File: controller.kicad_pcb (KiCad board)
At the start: 2 copper layers, 156.8 x 70.7 mm, 46 parts, among them J1 Conn_ST_STDC14, J2 USB_C_Receptacle_USB2.0_14P, SW1 SW_Push, SW10 SW_Push, SW11 SW_Push, SW2 SW_Push, SW3 SW_Push, SW4 SW_Push, SW5 SW_Push, SW6 SW_Push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

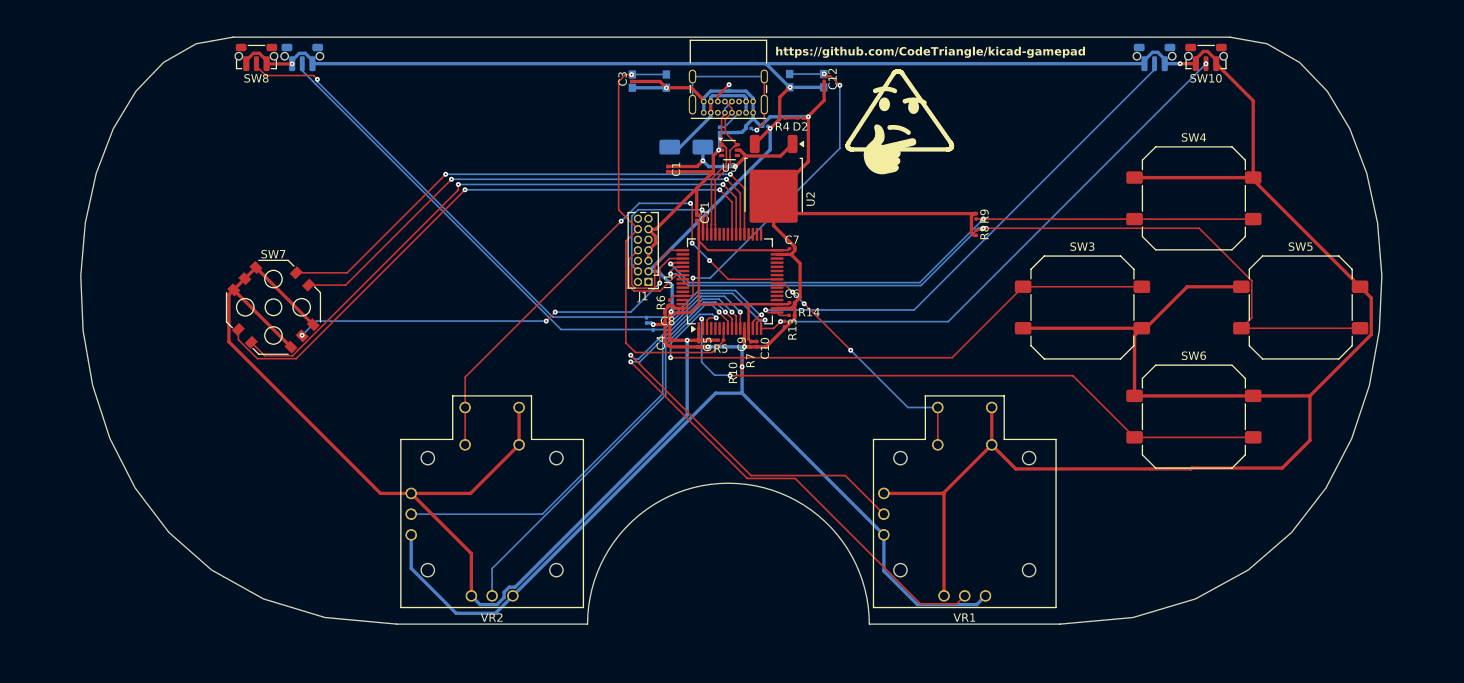
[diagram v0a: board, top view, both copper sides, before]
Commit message: add start and select + resistors to all other buttons
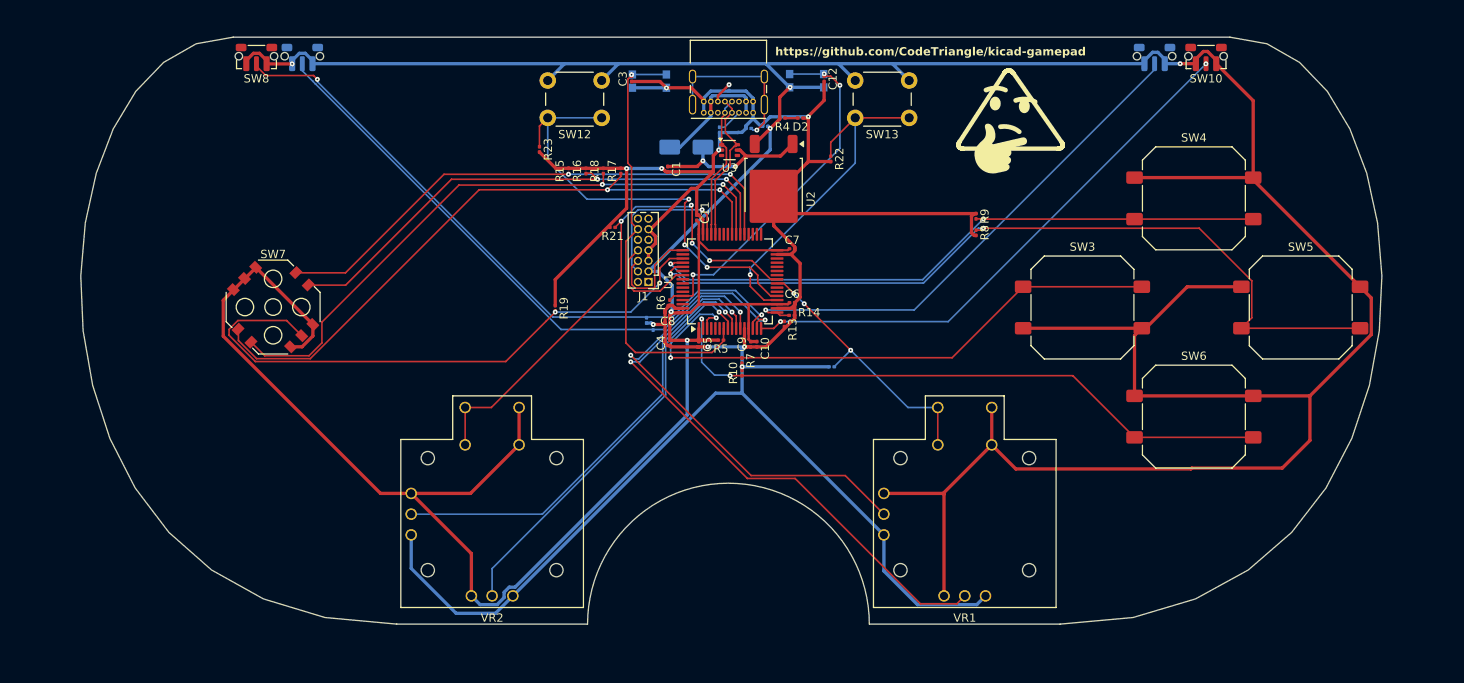
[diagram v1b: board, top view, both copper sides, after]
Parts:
- added R15: 10k, Resistor_SMD:R_0201_0603Metric, F.Cu at (118.0, 78.3)
- added R16: 10k, Resistor_SMD:R_0201_0603Metric, F.Cu at (120.1, 78.3)
- added R17: 10k, Resistor_SMD:R_0201_0603Metric, F.Cu at (124.3, 78.3)
- added R18: 10k, Resistor_SMD:R_0201_0603Metric, F.Cu at (122.2, 78.3)
- added R19: 10k, Resistor_SMD:R_0201_0603Metric, F.Cu at (116.4, 94.8)
- added R20: 10k, Resistor_SMD:R_0201_0603Metric, B.Cu at (149.7, 101.9)
- added R21: 10k, Resistor_SMD:R_0201_0603Metric, F.Cu at (123.3, 85.1)
- added R22: 10k, Resistor_SMD:R_0201_0603Metric, F.Cu at (149.6, 76.8)
- added R23: 10k, Resistor_SMD:R_0201_0603Metric, F.Cu at (114.5, 75.7)
- added SW12: SW_Push, Button_Switch_THT:SW_PUSH_6mm, F.Cu at (122.0, 71.9)
- added SW13: SW_Push, Button_Switch_THT:SW_PUSH_6mm, F.Cu at (159.0, 71.9)
- moved SW7 0.05 mm to (82.4, 94.7)
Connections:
- R7 pad 1: ButtonLeft -> GND
- R7 pad 2: GND -> ButtonLeft
- U1 pad 20: SelectINS -> ButtonStart
- U1 pad 21: SPI1_SCK -> ButtonSelect
- U1 pad 22: SPI1_MISO -> unconnected-(U1-PA6-Pad22)
- U1 pad 23: SPI1_MOSI -> unconnected-(U1-PA7-Pad23)
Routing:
- net ButtonSelect: track 0.00 -> 54.4 mm, vias 0 -> 3
- net GND: track 270.2 -> 320.1 mm, vias 7 -> 9
- net ButtonStart: track 0.00 -> 41.8 mm, vias 0 -> 1
- net DPadCenter: track 50.7 -> 72.8 mm, vias 4 -> 2
- net +3.3V: track 566.1 -> 573.0 mm
- net RightClick: track 30.1 -> 32.8 mm
- net DPadLeft: track 74.6 -> 77.2 mm
- net LeftClick: track 60.9 -> 63.5 mm
- net DPadDown: track 73.2 -> 75.6 mm
- net DPadRight: track 63.0 -> 64.7 mm
- net nRST: track 53.5 -> 52.0 mm

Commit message: fix ERC and add metadata
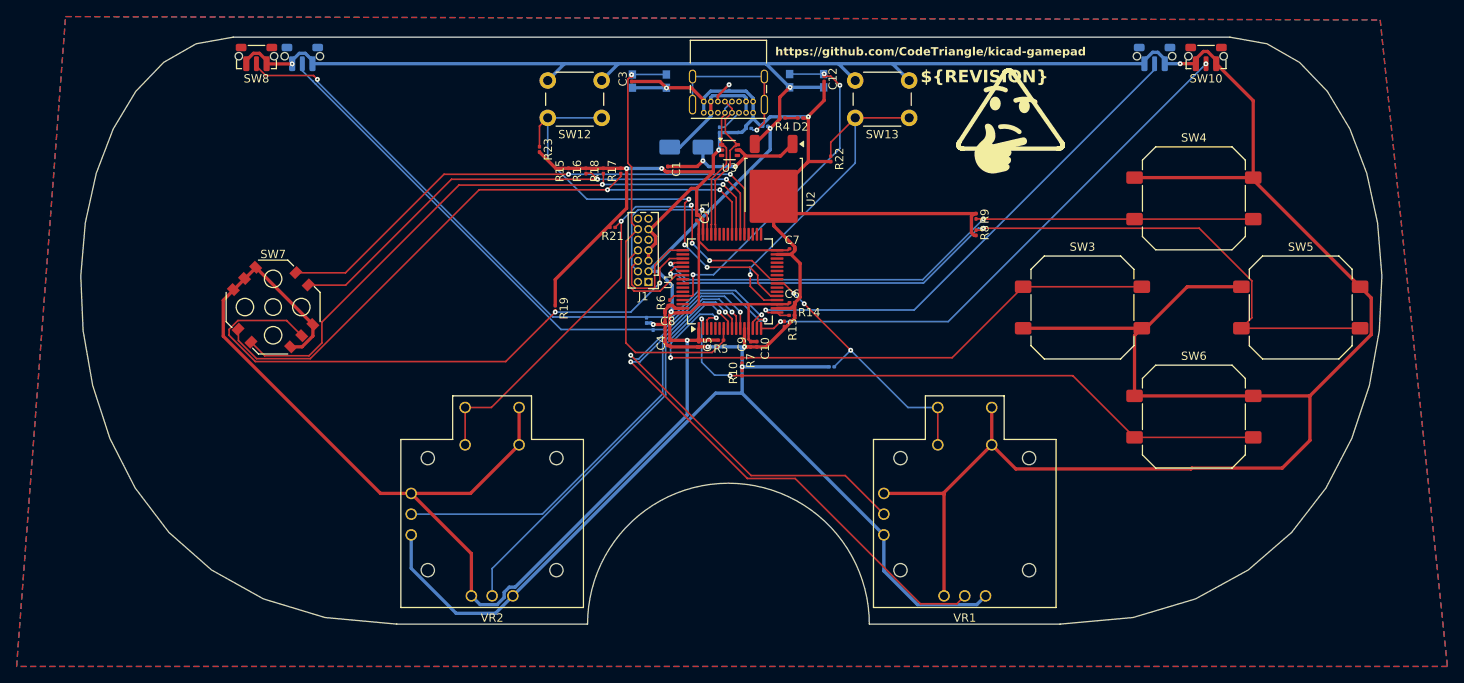
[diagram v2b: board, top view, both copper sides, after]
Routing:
- added copper zone on B.Cu, net GND
- added copper zone on F.Cu, net GND
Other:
- board text added: "${REVISION}"
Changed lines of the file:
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@@
 	)
 	(paper "A4")
+	(title_block
+		(title "${TITLE}")
+		(date "2025-11-02")
+		(rev "${REVISION}")
+		(company "USU")
+		(comment 1 "${AUTHOR}")
+	)
 	(layers
 		(0 "F.Cu" signal)
@@
 		)
 	)
+	(property "AUTHOR" "Richard Snider (CodeTriangle)")
+	(property "REVISION" "R1.0-A")
+	(property "TITLE" "USB Gamepad Controller")
 	(net 0 "")
 	(net 1 "+5V")
@@
 		(layer "Edge.Cuts")
 	)
+	(gr_text "${REVISION}"
+		(at 160.4 67.8 0)
+		(layer "F.SilkS")
+		(effects
+			(font
+				(size 1.5 1.5)
+				(thickness 0.3)
+				(bold yes)
+			)
+			(justify left bottom)
+		)
+	)
 	(gr_text "https://github.com/CodeTriangle/kicad-gamepad"
 		(at 142.9 64.5 0)
@@
 		(net 67)
 	)
+	(zone
+		(net 2)
+		(net_name "GND")
+		(layers "F.Cu" "B.Cu")
+		(hatch edge 0.5)
+		(connect_pads
+			(clearance 0.5)
+		)
+		(min_thickness 0.25)
+		(filled_areas_thickness no)
+		(fill yes
+			(thermal_gap 0.5)
+			(thermal_bridge_width 0.5)
+		)
+		(polygon
+			(pts
+				(xy 57.4 59.7) (xy 215.8 60.1) (xy 223.9 138) (xy 51.5 138)
+			)
+		)
+	)
 	(group ""

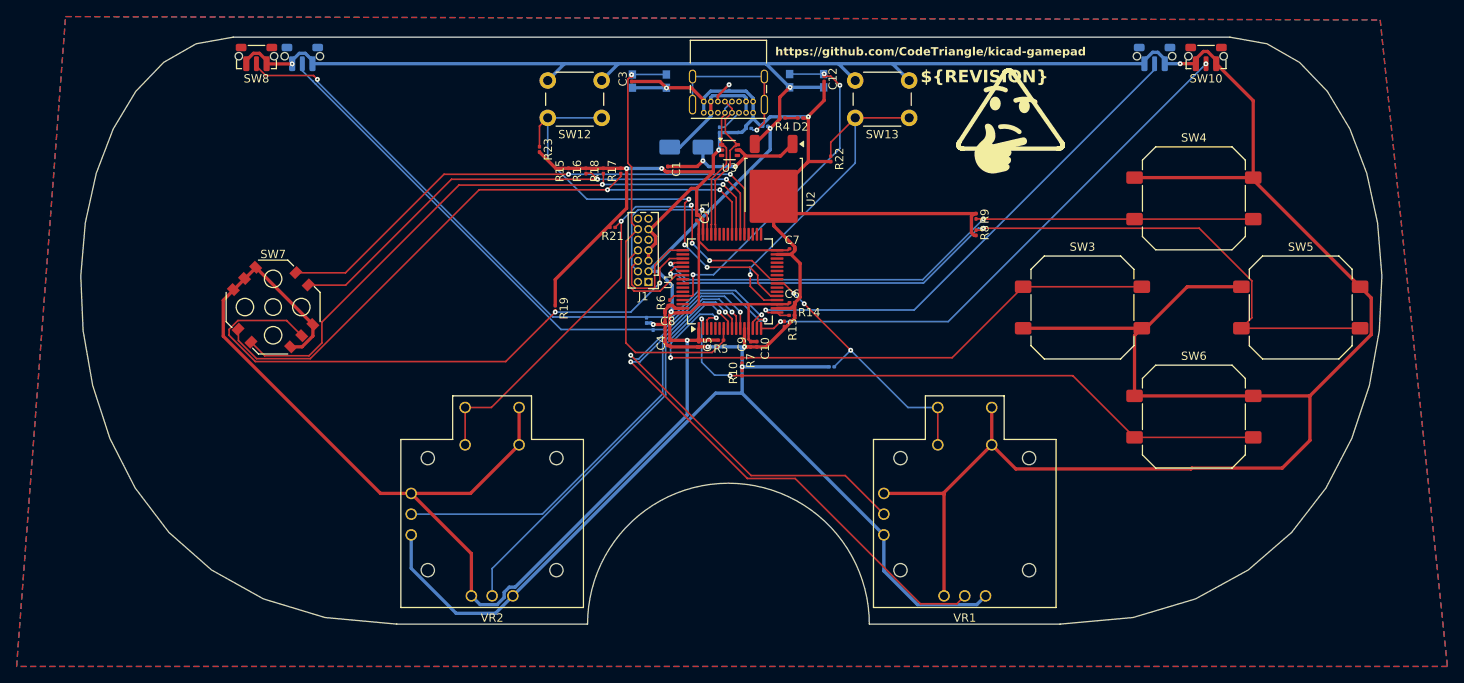
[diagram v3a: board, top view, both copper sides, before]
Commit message: update pcb to reflect new footprints
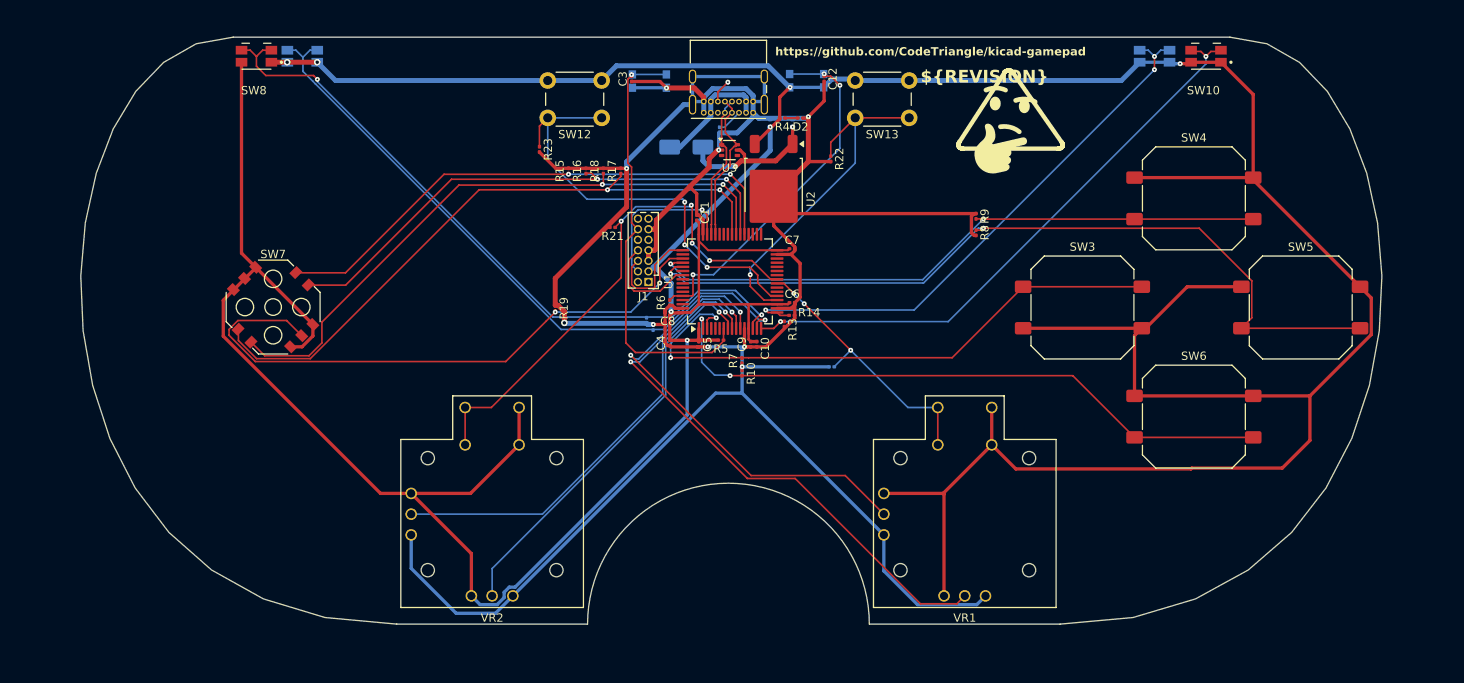
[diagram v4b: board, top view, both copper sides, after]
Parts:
- removed R3: 5.1k, Resistor_SMD:R_0201_0603Metric
- C1: value 10uF -> 10u; footprint Capacitor_SMD:C_0201_0603Metric -> Capacitor_SMD:C_0402_1005Metric; moved to B.Cu
- C12, C3: value 100nF -> 100n
- C2: value 10uF -> 10u; footprint Capacitor_SMD:C_0201_0603Metric -> Capacitor_SMD:C_0402_1005Metric
- SW10, SW11, SW8, SW9: footprint Button_Switch_SMD:SW_Push_1P1T-MP_NO_Horizontal_Alps_SKRTLAE010 -> EVQ-P7A01P:SW_EVQ-P7A01P_Single
- moved C1 16.0 mm to (145.0, 72.5), turned to 90 degrees
- moved C2 0.73 mm to (142.3, 72.5), turned to -90 degrees
- moved R2 0.35 mm to (137.2, 68.0)
- turned R7 to 90 degrees
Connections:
- J2 pad S1: Net-(J2-SHIELD) -> GND
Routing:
- net GND: track 320.1 -> 351.8 mm
- net Net-(J2-SHIELD): track 19.6 -> 0.00 mm, vias 1 -> 0
- net RightTriggerBottom: track 62.6 -> 67.8 mm, vias 1 -> 3
- net RightTriggerTop: track 67.3 -> 72.4 mm
- net LeftTriggerTop: track 78.7 -> 83.7 mm
- net LeftTriggerBottom: track 74.7 -> 79.8 mm
- net +5V: track 19.7 -> 17.8 mm
- net ButtonSelect: track 54.4 -> 53.5 mm
- net +3.3V: track 573.0 -> 573.5 mm, vias 6 -> 7
- removed copper zone on B.Cu, net GND
- removed copper zone on F.Cu, net GND

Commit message: some minor trace changes
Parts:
- moved R17 0.10 mm to (122.1, 78.3)
- moved R15 0.10 mm to (117.9, 78.3)
- moved R16 0.10 mm to (120.0, 78.3)
- moved R18 0.10 mm to (124.2, 78.3)
- renumbered R18 to R17, R17 to R18
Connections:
- R8 pad 1: ButtonRight -> unconnected-(R8-Pad1)
- R8 pad 2: GND -> unconnected-(R8-Pad2)
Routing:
- net +3.3V: track 573.5 -> 563.6 mm, vias 7 -> 9
- net GND: track 351.8 -> 343.2 mm
- net LeftTriggerTop: track 83.7 -> 82.7 mm
- net DPadRight: track 64.7 -> 63.6 mm
- net BOOT0: track 43.6 -> 44.3 mm
- net DPadLeft: track 77.2 -> 76.6 mm
- net ButtonSelect: vias 3 -> 1
- net LeftClick: vias 4 -> 2
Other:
- board text added: "BOOT"

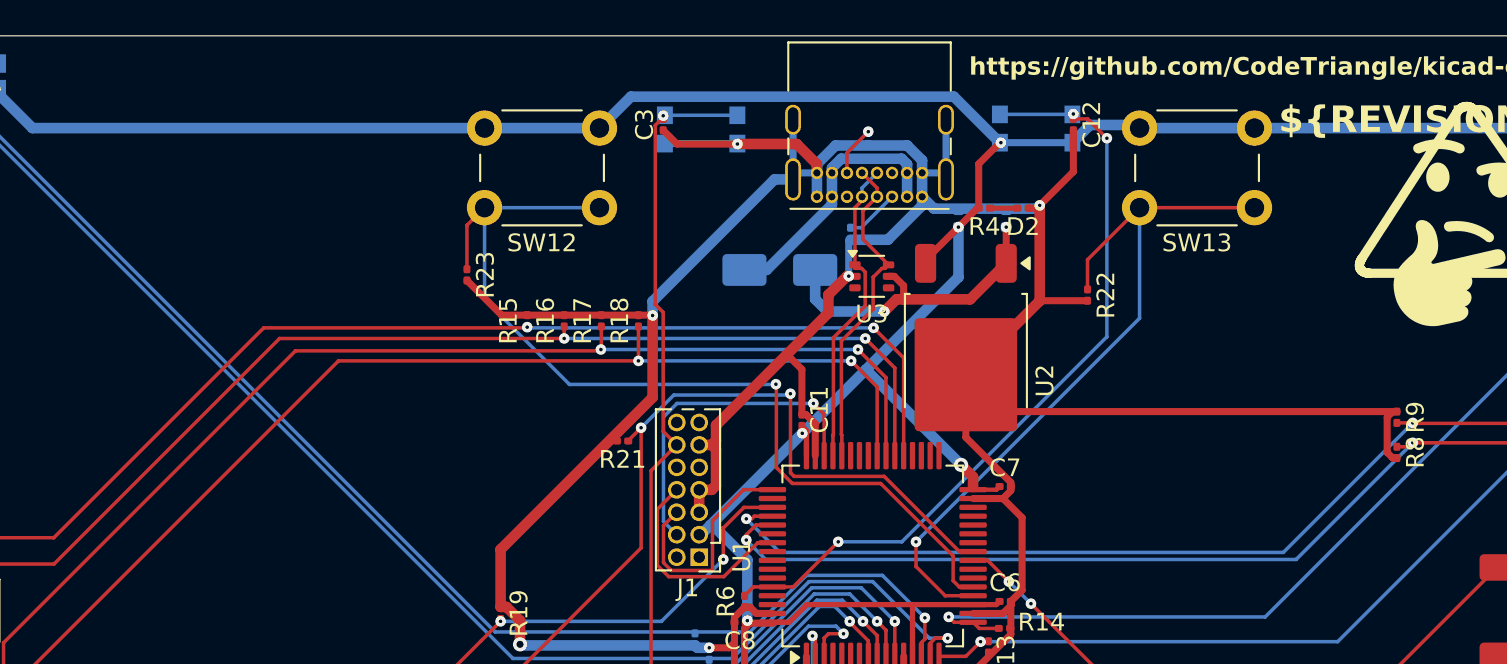
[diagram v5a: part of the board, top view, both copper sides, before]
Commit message: add pcbway logo and some more trace modifications
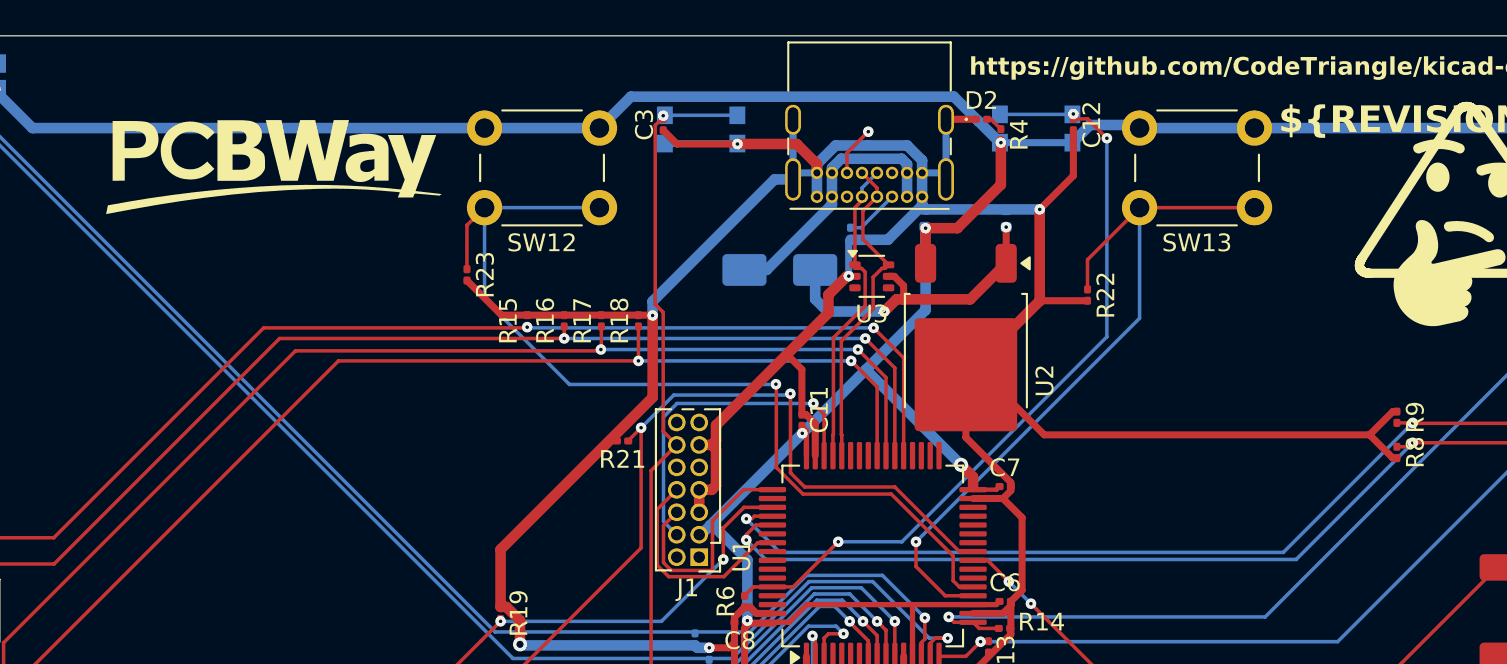
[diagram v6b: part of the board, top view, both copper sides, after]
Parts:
- moved D2 5.55 mm to (143.6, 66.9), turned to 0 degrees
- moved R4 4.25 mm to (144.7, 67.8), turned to 90 degrees
- moved C2 1.90 mm to (140.4, 72.5)
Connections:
- R8 pad 1: unconnected-(R8-Pad1) -> ButtonRight
- R8 pad 2: unconnected-(R8-Pad2) -> GND
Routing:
- net GND: track 343.2 -> 346.9 mm
- net +3.3V: track 563.6 -> 564.1 mm
- net Net-(D2-A): track 1.55 -> 1.01 mm
